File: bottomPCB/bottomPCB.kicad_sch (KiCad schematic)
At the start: 15 parts, among them P1 Pfostenstecker_8_2x4, U1 ESP32-WROOM-32, U2 Pfostenstecker_6_2x3

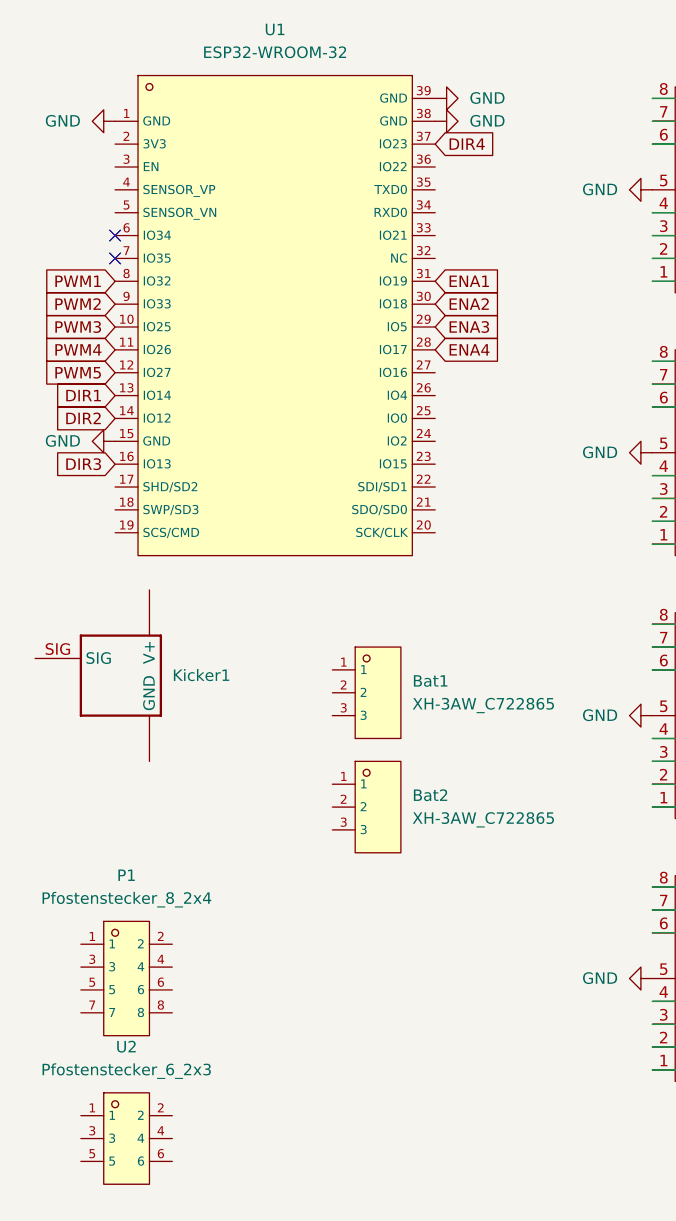
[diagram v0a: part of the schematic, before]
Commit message: added programmer
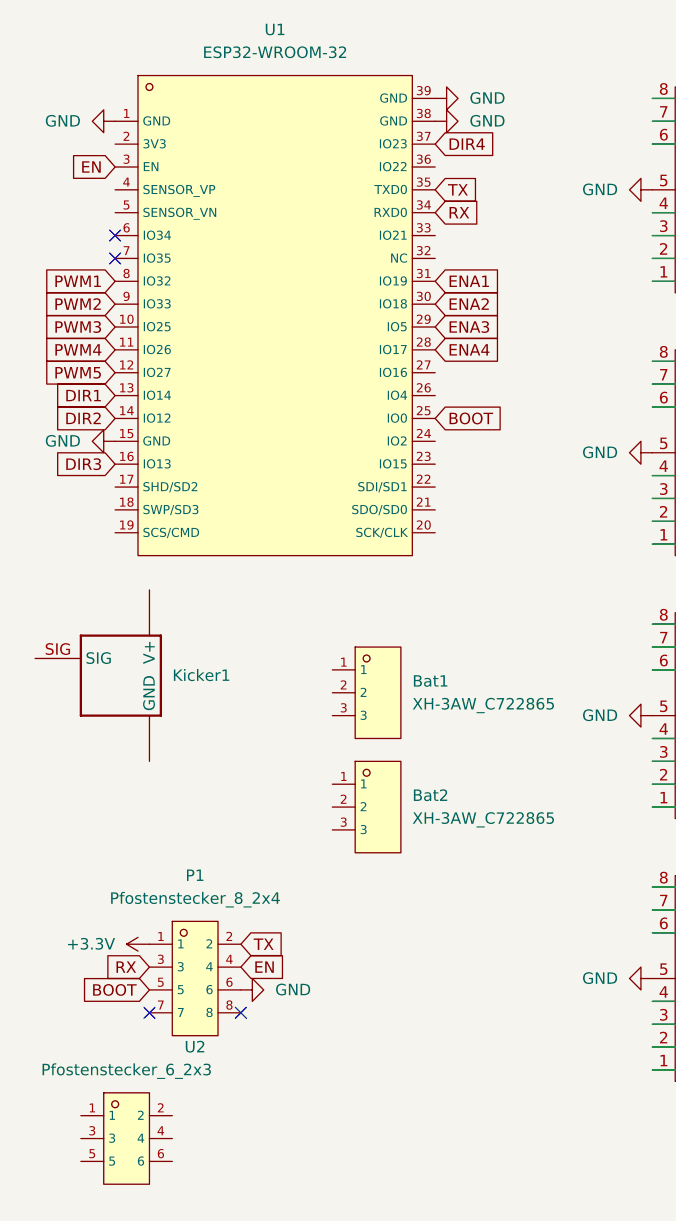
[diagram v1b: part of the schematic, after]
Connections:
- net GND: now also P1.6
- net +3.3V: now reaches P1.1
- net TX: now reaches P1.2
- net TX: now also U1.35 (TXD0)
- net RX: now reaches P1.3
- net RX: now also U1.34 (RXD0)
- net EN: now reaches P1.4
- net EN: now also U1.3 (EN)
- net BOOT: now reaches P1.5
- net BOOT: now also U1.25 (IO0)
- no-connect marks 6 -> 8
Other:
- moved on the sheet: P1

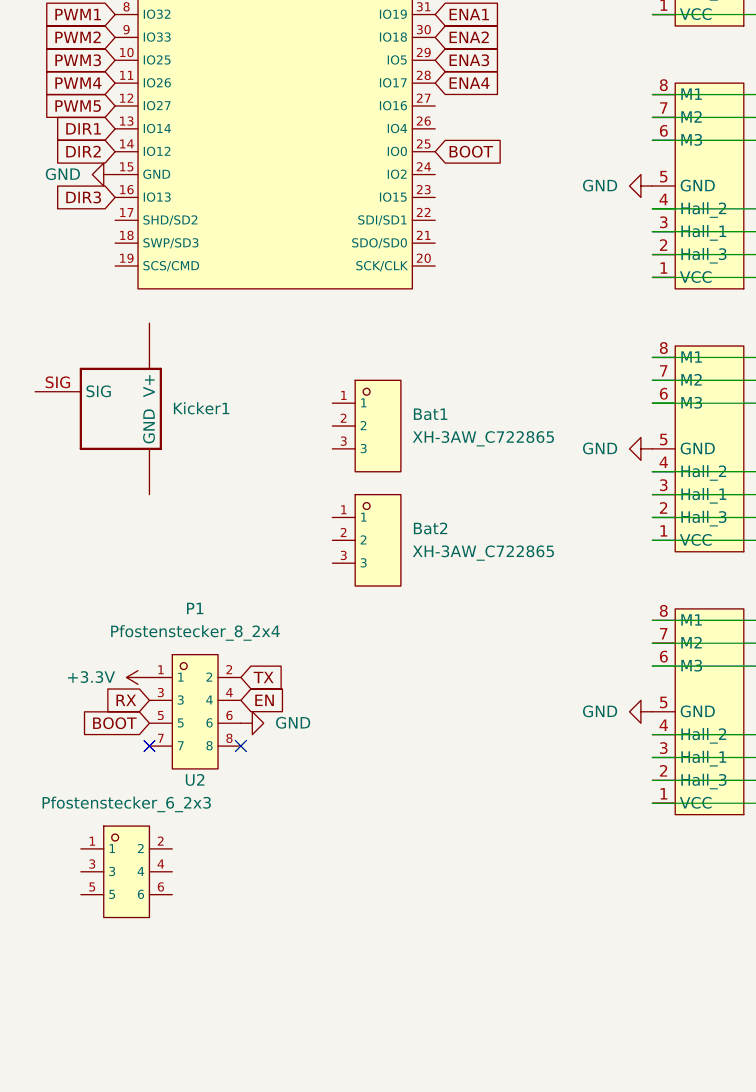
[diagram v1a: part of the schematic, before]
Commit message: added kicker
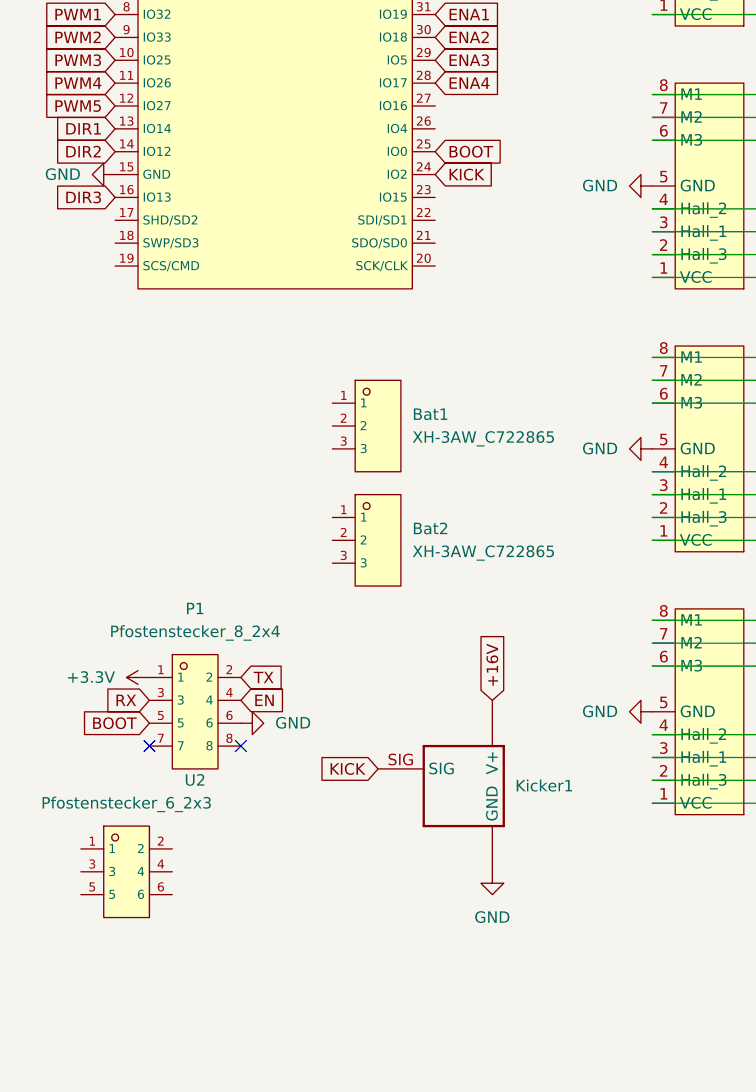
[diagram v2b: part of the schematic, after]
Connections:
- net +16V: now also Kicker1.V+1 (V+), Kicker1.V+2 (V+), Kicker1.V+3 (V+)
- net GND: now also Kicker1.GND1 (GND), Kicker1.GND2 (GND), Kicker1.GND3 (GND), Kicker1.GND4 (GND), Kicker1.GND5 (GND), Kicker1.GND6 (GND), Kicker1.GND7 (GND), Kicker1.GND8 (GND)
- net KICK: now reaches U1.24 (IO2)
- net KICK: now also Kicker1.SIG
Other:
- moved on the sheet: Kicker1
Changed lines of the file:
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@@
+		)
+	)
+	(global_label "KICK"
+		(shape input)
+		(at 57.15 57.15 0)
+		(fields_autoplaced yes)
+		(effects
+			(font
+				(size 1.27 1.27)
+			)
+			(justify left)
+		)
+		(property "Intersheetrefs" "${INTERSHEET_REFS}"
+			(at 64.55 57.15 0)
+			(effects
+				(font
+					(size 1.27 1.27)
+				)
+				(justify left)
+				(hide yes)
+			)
 		)
 	)
@@
 	(global_label "+16V"
 		(shape input)
-		(at 130.81 20.32 0)
+		(at 63.5 115.57 90)
 		(fields_autoplaced yes)
 		(effects
@@
 		)
 		(property "Intersheetrefs" "${INTERSHEET_REFS}"
+			(at 63.5 107.5048 90)
+			(effects
+				(font
+					(size 1.27 1.27)
+				)
+				(justify left)
+				(hide yes)
+			)
+		)
+	)
+	(global_label "+16V"
+		(shape input)
+		(at 130.81 20.32 0)
+		(fields_autoplaced yes)
+		(effects
+			(font
+				(size 1.27 1.27)
+			)
+			(justify left)
+		)
+		(property "Intersheetrefs" "${INTERSHEET_REFS}"
 			(at 138.8752 20.32 0)
 			(effects
@@
 		)
 	)
+	(global_label "KICK"
+		(shape input)
+		(at 50.8 123.19 180)
+		(fields_autoplaced yes)
+		(effects
+			(font
+				(size 1.27 1.27)
+			)
+			(justify right)
+		)
+		(property "Intersheetrefs" "${INTERSHEET_REFS}"
+			(at 43.4 123.19 0)
+			(effects
+				(font
+					(size 1.27 1.27)
+				)
+				(justify right)
+				(hide yes)
+			)
+		)
+	)
 	(global_label "EN"
 		(shape input)
@@
 	)
 	(symbol
+		(lib_id "bohlebots.lib:GND")
+		(at 63.5 134.62 0)
+		(unit 1)
+		(exclude_from_sim no)
+		(in_bom yes)
+		(on_board yes)
+		(dnp no)
+		(fields_autoplaced yes)
+		(property "Reference" "#PWR016"
+			(at 63.5 140.97 0)
+			(effects
+				(font
+					(size 1.27 1.27)
+				)
+				(hide yes)
+			)
+		)
+		(property "Value" "GND"
+			(at 63.5 139.7 0)
+			(effects
+				(font
+					(size 1.27 1.27)
+				)
+			)
+		)
+		(property "Footprint" ""
+			(at 63.5 134.62 0)
+			(effects
+				(font
+					(size 1.27 1.27)
+				)
+				(hide yes)
+			)
+		)
+		(property "Datasheet" ""
+			(at 63.5 134.62 0)
+			(effects
+				(font
+					(size 1.27 1.27)
+				)
+				(hide yes)
+			)
+		)
+		(property "Description" "Power symbol creates a global label with name \"GND\" , ground"
+			(at 63.5 134.62 0)
+			(effects
+				(font
+					(size 1.27 1.27)
+				)
+				(hide yes)
+			)
+		)
+		(pin "1"
+		)
+		(instances
+			(project "bottomPCB"
+				(path "/530b96b6-d439-440e-a48e-82f0fe8f4bb1"
+					(reference "#PWR016")
+					(unit 1)
+				)
+			)
+		)
+	)
+	(symbol
 		(lib_id "bohlebots.lib:XH-3AW_C722865")
 		(at 50.8 85.09 0)
@@
 	(symbol
 		(lib_id "bohlebots.lib:KICKER")
-		(at 25.4 81.28 0)
+		(at 63.5 123.19 0)
 		(unit 1)
 		(exclude_from_sim no)
@@
 		(fields_autoplaced yes)
 		(property "Reference" "Kicker1"
-			(at 27.94 83.1849 0)
+			(at 66.04 125.0949 0)
 			(effects
 				(font
@@
 		)
 		(property "Value" "~"
-			(at 25.4 81.28 0)
+			(at 63.5 123.19 0)
 			(effects
 				(font
@@
 		)
 		(property "Footprint" "BohleBots:KICKER"
-			(at 15.24 90.17 0)
+			(at 53.34 132.08 0)
 			(effects
 				(font
@@
 		)
 		(property "Datasheet" ""
-			(at 25.4 81.28 0)
+			(at 63.5 123.19 0)
 			(effects
 				(font
@@
 		)
 		(property "Description" ""
-			(at 25.4 81.28 0)
-			(effects
-				(font
+			(at 63.5 123.19 0)
+			(effects
+				(font

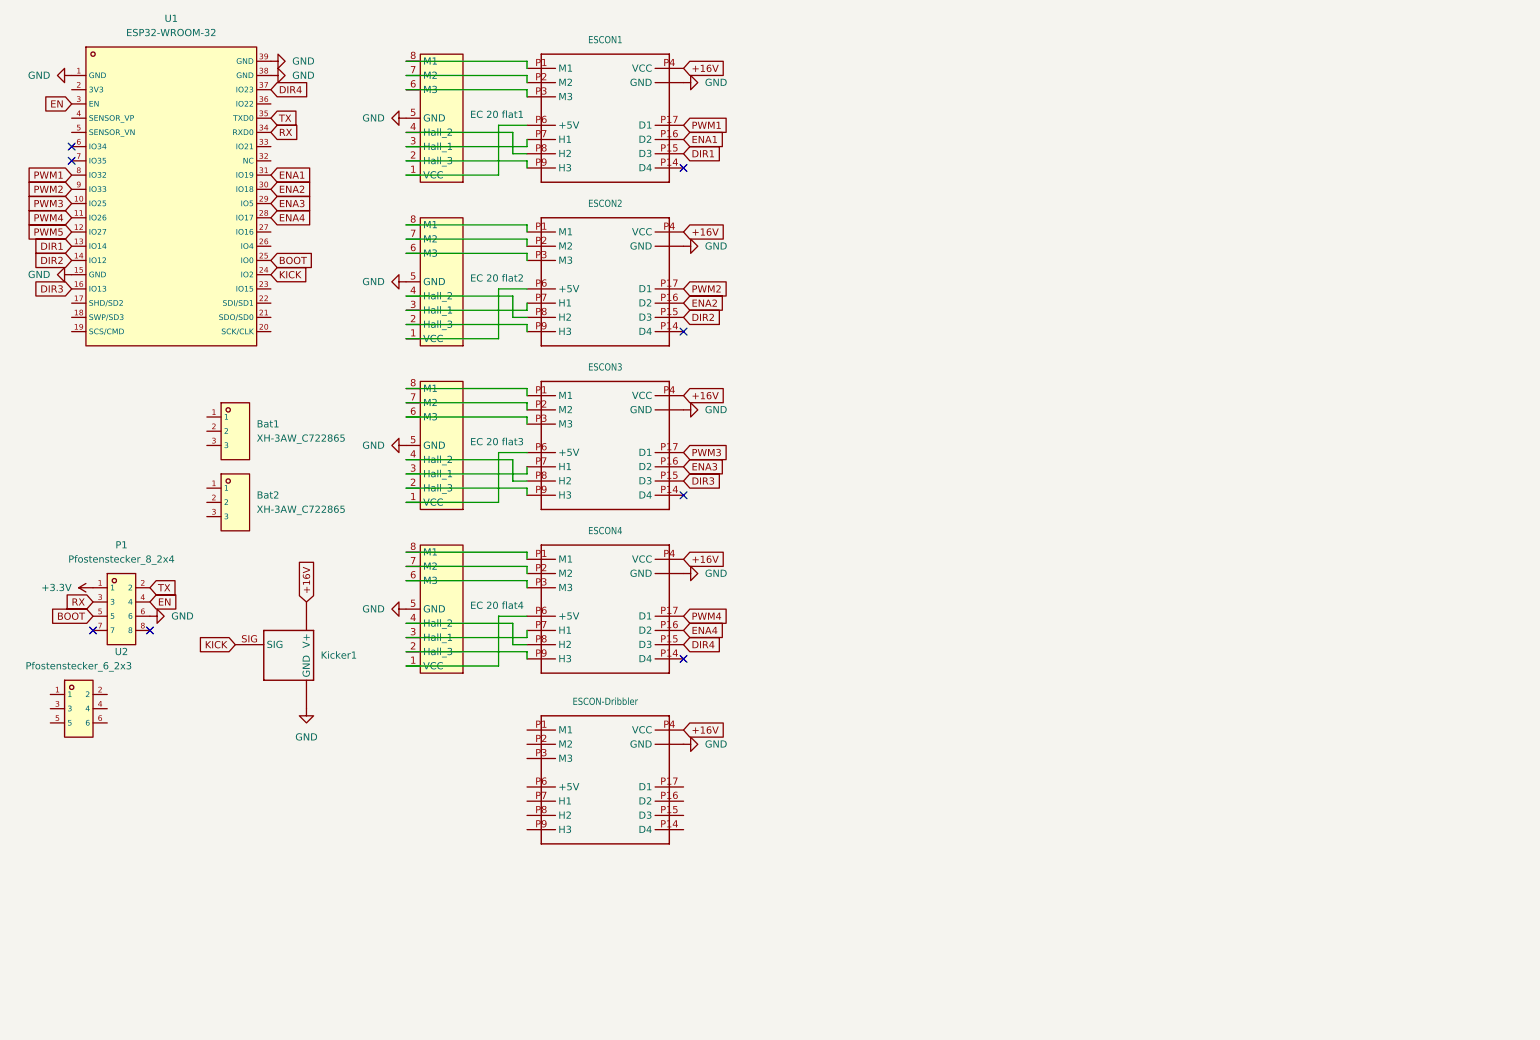
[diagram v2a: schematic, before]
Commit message: simlified to one header pin
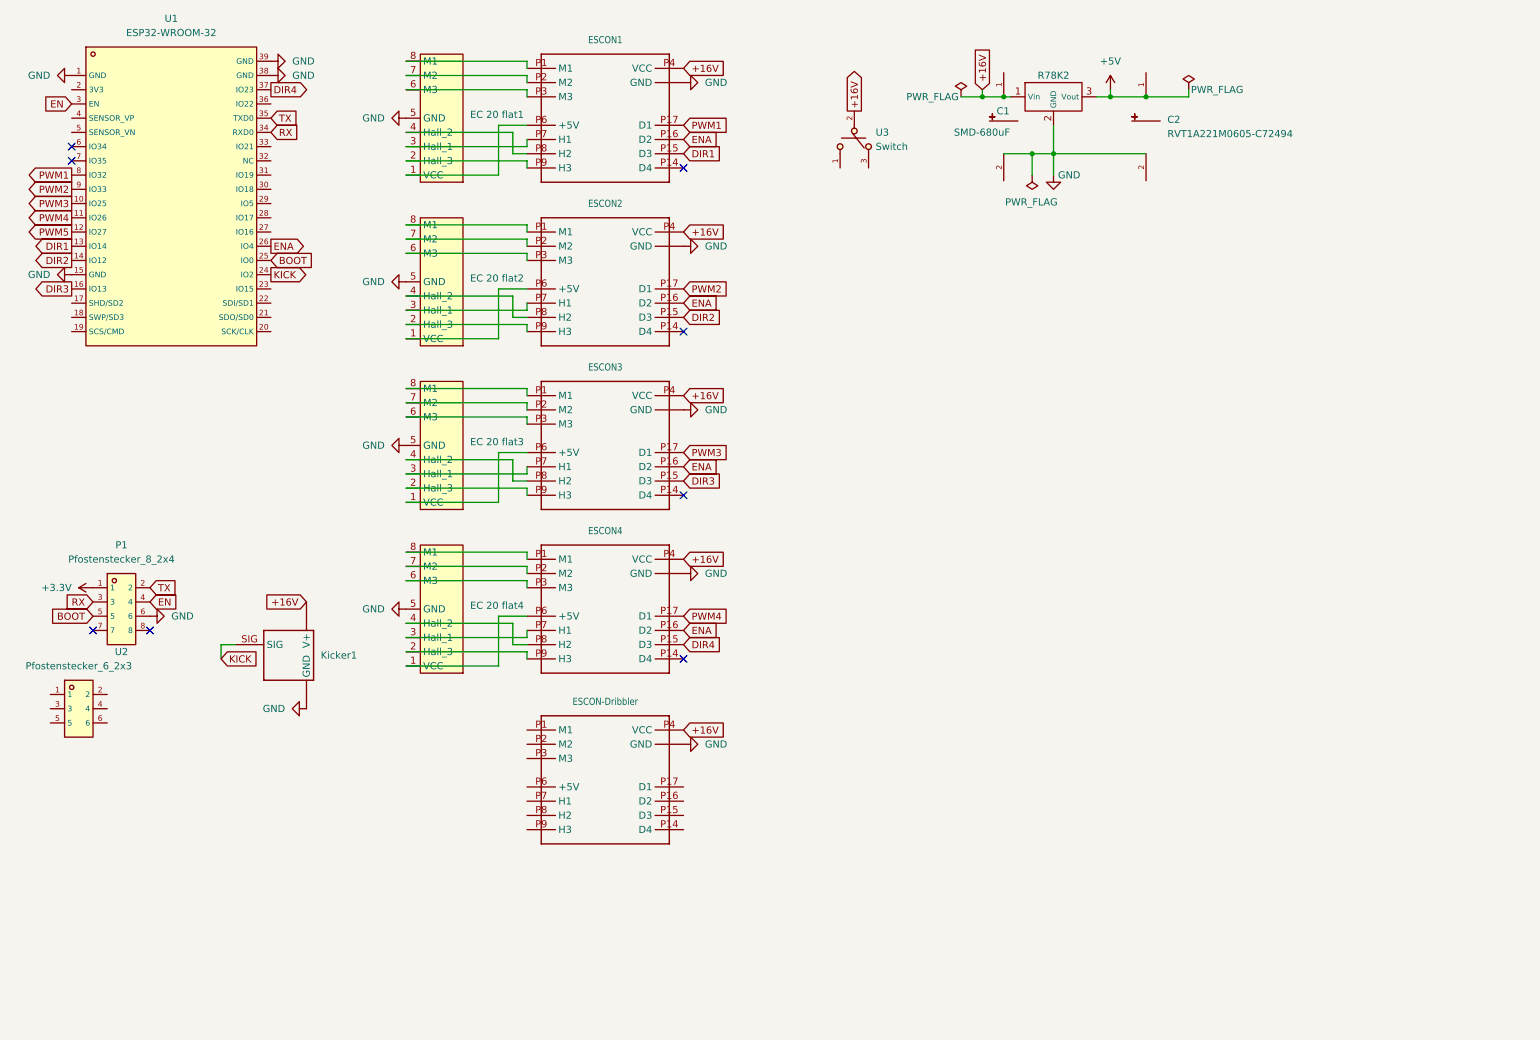
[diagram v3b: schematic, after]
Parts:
- removed Bat1, Bat2: XH-3AW_C722865, BohleBots:CONN-TH_XH-3AW-C722865, symbol bohlebots.lib:XH-3AW_C722865
- added C1: SMD-680uF, BohleBots:CAP-SMD_BD10.0-L10.3-W10.3-LS11.3-FD, symbol Bohlebots:SMD-680uF
- added C2: RVT1A221M0605-C72494, BohleBots:CAP-SMD_BD10.0-L10.3-W10.3-LS11.3-FD, symbol Bohlebots:SMD-220uF_50V
- added R78K2: ~, BohleBots:R785K, symbol Bohlebots:R78K5
- added U3: Switch, BohleBots:SW-TH_MT-0-103-A101-M200-RS, symbol bohlebots.lib:Switch
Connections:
- net +16V: now also C1.1, R78K2.1 (Vin), U3.2
- net GND: now also C1.2, C2.2, R78K2.2 (GND)
- net ENA: now reaches U1.26 (IO4)
- net ENA: now also ESCON1.P16 (D2), ESCON2.P16 (D2), ESCON3.P16 (D2), ESCON4.P16 (D2)
- net ENA1: no longer names the net of U1.31 (IO19)
- net ENA1: no longer ESCON1.P16 (D2)
- net ENA2: no longer names the net of U1.30 (IO18)
- net ENA2: no longer ESCON2.P16 (D2)
- net ENA3: no longer names the net of U1.29 (IO5)
- net ENA3: no longer ESCON3.P16 (D2)
- net ENA4: no longer names the net of U1.28 (IO17)
- net ENA4: no longer ESCON4.P16 (D2)
- new net +5V: C2.1, R78K2.3 (Vout)
